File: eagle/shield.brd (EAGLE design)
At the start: 68.6 x 53.3 mm, 31 parts, among them IC1 REG1117

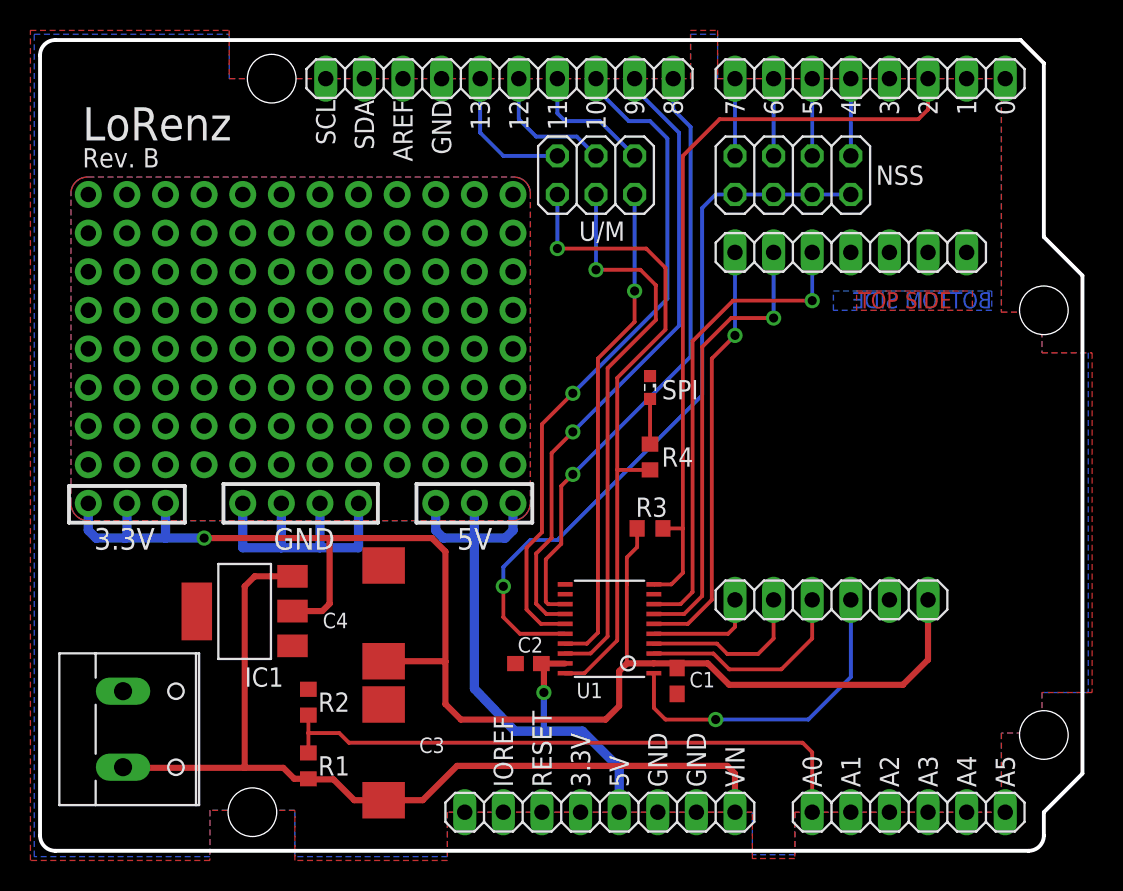
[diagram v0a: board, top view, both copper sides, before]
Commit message: Shield layout update
Added two separate TXB0104 instead of one TXB0108 (signal direction issues), added EN solder jumper for LED, removed battery level measurement, increased the protoyping area size, general layout changes for easier soldering.
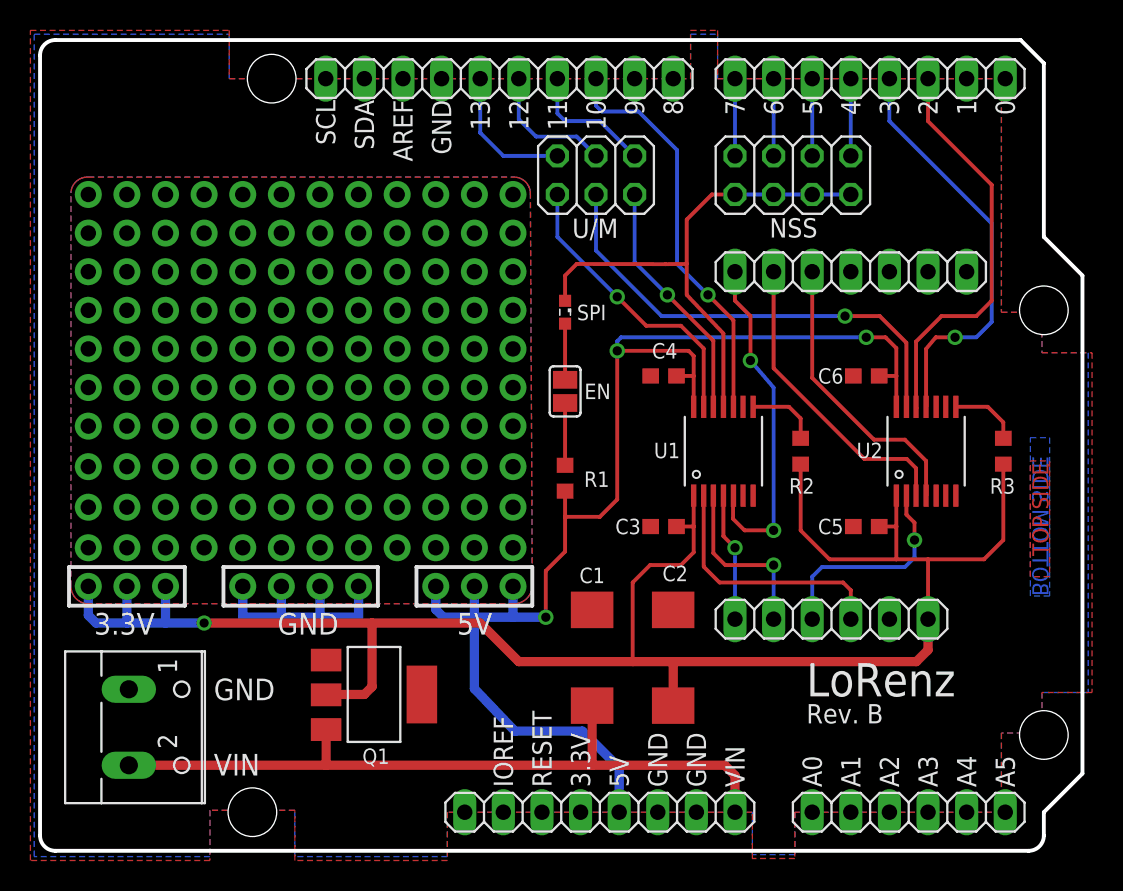
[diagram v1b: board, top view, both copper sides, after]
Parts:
- removed IC1: REG1117, burr-brown:SOT223
- removed R4: 1k, rcl:R0603
- removed U$1: PINHD-1X4, adafruit:1X04-CLEANBIG
- added C5, C6: 0.1 uF, rcl:C0603
- added EN: (no value), jumper:SJ
- added JP10: (no value), adafruit:1X12-CB
- added JP12: PINHD-1X4, adafruit:1X04-CLEANBIG
- added JP13: (no value), adafruit:1X03-CLEANBIG
- added Q1: REG1117, burr-brown:SOT223
- added U2: TXB0104PWR, Texas Instruments_By_element14_Batch_1:SOP65P640X120-14N
- C1, C2: value 0.1 uF -> 100 uF; device rcl:C0603 -> rcl:SMC_D
- C3, C4: value 100 uF -> 0.1 uF; device rcl:SMC_D -> rcl:C0603
- JP9: device adafruit:1X03-CLEANBIG -> adafruit:1X12-CB
- R1: value 3M3 -> 1k
- R2: value 1M -> 10k
- U1: value (none) -> TXB0104PWR; device adafruit:TSSOP20 -> Texas Instruments_By_element14_Batch_1:SOP65P640X120-14N
- moved R2 36.4 mm to (50.2, 26.4), turned to 90 degrees
- moved R1 25.4 mm to (34.7, 24.6), turned to 90 degrees
- moved C4 24.1 mm to (41.1, 31.4), turned to 0 degrees
- moved R3 23.8 mm to (63.5, 26.4), turned to 90 degrees
- moved C3 23.7 mm to (41.1, 21.5), turned to 0 degrees
- moved U1 13.9 mm to (45.1, 26.4)
- moved JP9 11.4 mm to (17.3, 22.7)
- moved C2 9.53 mm to (41.8, 12.8), turned to 90 degrees
- moved SPI 7.47 mm to (34.7, 35.6)
- moved C1 5.79 mm to (36.4, 12.8), turned to 90 degrees
- moved JP11 5.46 mm to (28.7, 17.5)
- moved LORA2 1.27 mm to (53.5, 38.2)
- moved LORA1 1.27 mm to (52.2, 15.4)
- moved POWER1 0.40 mm to (7.24, 8.26)
- moved JP8 0.13 mm to (17.3, 25.4)
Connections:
- removed net 3V3: C1.1, C4.+, IC1.2, JP9.1, JP9.2, JP9.3, LORA1.6, R3.1, U1.2
- removed net 5V: ARDUINO-LU.5, C2.1, JP11.1, JP11.2, JP11.3, U1.19
- removed net A0: ARDUINO-LD.1, R1.1, R2.2
- removed net OE: ARDUINO-RD.6, R3.2, U1.10
- new net +3V3: C2.+, C3.2, C5.2, JP13.1, JP13.2, JP13.3, LORA1.6, Q1.2, R2.1, R3.1, U1.1, U2.1
- new net +5V: ARDUINO-LU.5, C4.2, C6.2, JP11.1, JP11.2, JP11.3, R1.1, U1.14, U2.14
- new net N$10: EN.1, R1.2
- new net N$11: R2.2, U1.8
- new net N$12: R3.2, U2.8
- net A_DIO0: now also ARDUINO-RD.6, U2.12; no longer ARDUINO-RU.9, U1.14
- net A_DIO1: now also ARDUINO-RD.5, U2.11; no longer ARDUINO-RU.10, U1.13
- net A_MISO: now also U2.13; no longer U1.18
- net A_MOSI: now also U1.12; no longer U1.17
- net A_NSS: now also SPI.C, U1.11; no longer U1.16
- net A_RESET: now also U1.10; no longer U1.15
- net A_SCK: now also U1.13; no longer R4.2, U1.20
- net GND: now also C1.-, C2.-, C3.1, C4.1, C5.1, C6.1, JP12.1, JP12.2, JP12.3, JP12.4, Q1.1, U1.7, U2.7; no longer C1.2, C2.2, C3.-, C4.-, IC1.1, R2.1, SPI.C, U$1.1, U$1.2, U$1.3, U$1.4, U1.11
- net L_DIO0: now also U2.3; no longer U1.7
- net L_DIO1: now also U2.4; no longer U1.8
- net L_MISO: now also U2.2; no longer U1.3
- net L_MOSI: now also U1.3; no longer U1.4
- net L_NSS: now also U1.4; no longer U1.5
- net L_RESET: now also U1.5; no longer U1.6
- net L_SCK: now also U1.2; no longer U1.1
- net N$4: now also EN.2; no longer R4.1
- net VIN: now also C1.+, Q1.3; no longer C3.+, IC1.3, R1.2
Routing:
- net +3V3: track 0.00 -> 124.1 mm, vias 0 -> 1
- net 3V3: track 101.4 -> 0.00 mm, vias 1 -> 0
- net +5V: track 0.00 -> 88.9 mm, vias 0 -> 3
- net OE: track 50.4 -> 0.00 mm
- net 5V: track 42.0 -> 0.00 mm, vias 1 -> 0
- net A0: track 40.2 -> 0.00 mm
- net A_SCK: track 43.5 -> 19.3 mm
- net A_RESET: track 44.5 -> 26.7 mm
- net A_MOSI: track 32.3 -> 16.1 mm
- net A_DIO0: track 41.8 -> 26.8 mm, vias 1 -> 0
- net A_NSS: track 48.0 -> 34.7 mm, vias 1 -> 0
- net L_DIO1: track 31.5 -> 19.0 mm, vias 1 -> 0
- net A_DIO1: track 40.2 -> 27.7 mm
- net VIN: track 60.2 -> 48.8 mm
- net L_DIO0: track 29.9 -> 20.3 mm, vias 1 -> 0
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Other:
- board text added: "C:/Users/Honza/Desktop/ATLAS/atlas_logo_notext_gs.bmp"

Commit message: Shield and breakout layout update
Added a gap to the pin headers on LoRa breakout board and the shield to enforce breakout orientation.
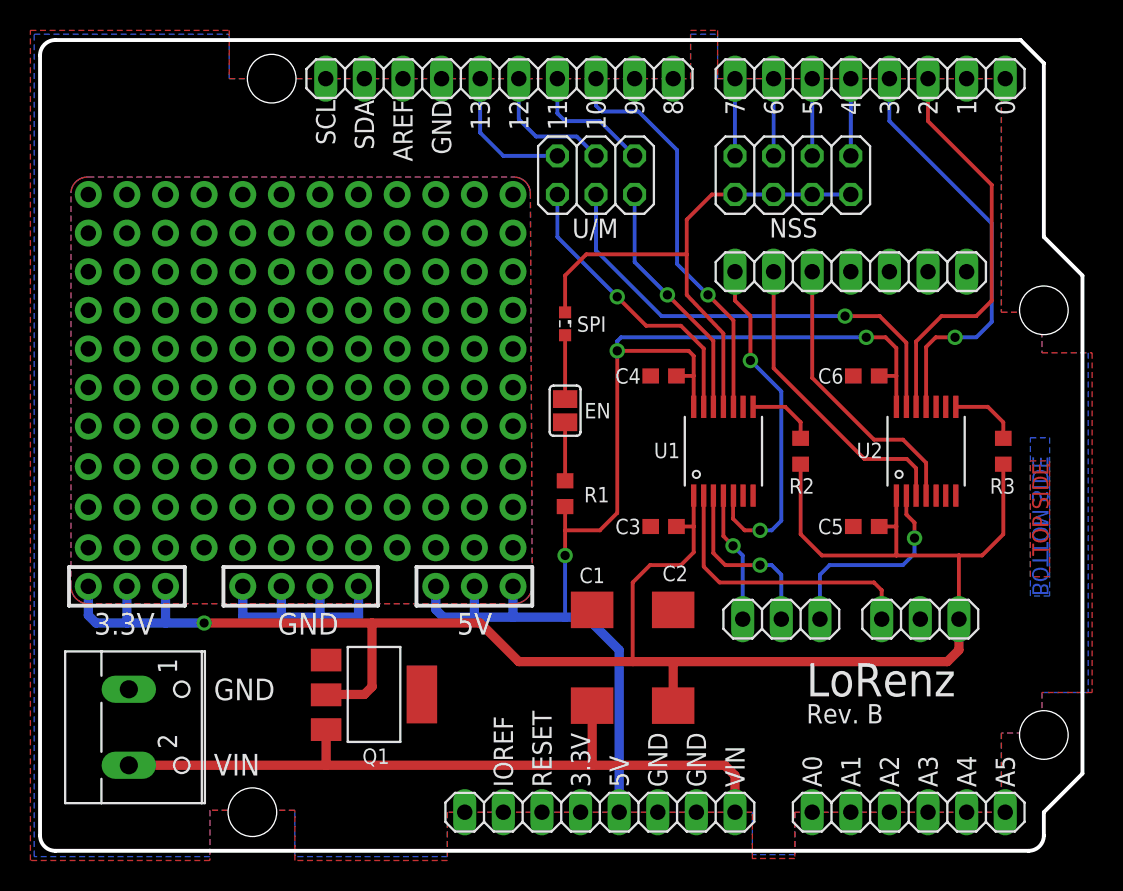
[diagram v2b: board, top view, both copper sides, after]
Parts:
- removed LORA1: (no value), pinhead:1X06
- added LORA1A, LORA1B: (no value), pinhead:1X03
- moved EN 1.27 mm to (34.7, 29.1)
- moved R1 1.02 mm to (34.7, 23.6)
- moved SPI 0.76 mm to (34.7, 34.8)
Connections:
- net +3V3: now also LORA1B.3; no longer LORA1.6
- net GND: now also LORA1B.2; no longer LORA1.5
- net L_MISO: now also LORA1A.3; no longer LORA1.3
- net L_MOSI: now also LORA1A.2; no longer LORA1.2
- net L_NSS: now also LORA1A.1; no longer LORA1.1
- net L_SCK: now also LORA1B.1; no longer LORA1.4
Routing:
- net +5V: track 88.9 -> 85.3 mm
- net L_SCK: track 16.9 -> 18.9 mm
- net +3V3: track 124.1 -> 125.8 mm
- net A_NSS: track 34.7 -> 35.8 mm
- net L_MISO: track 14.3 -> 13.8 mm
- net N$4: track 3.70 -> 4.20 mm

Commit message: Changed package of C2
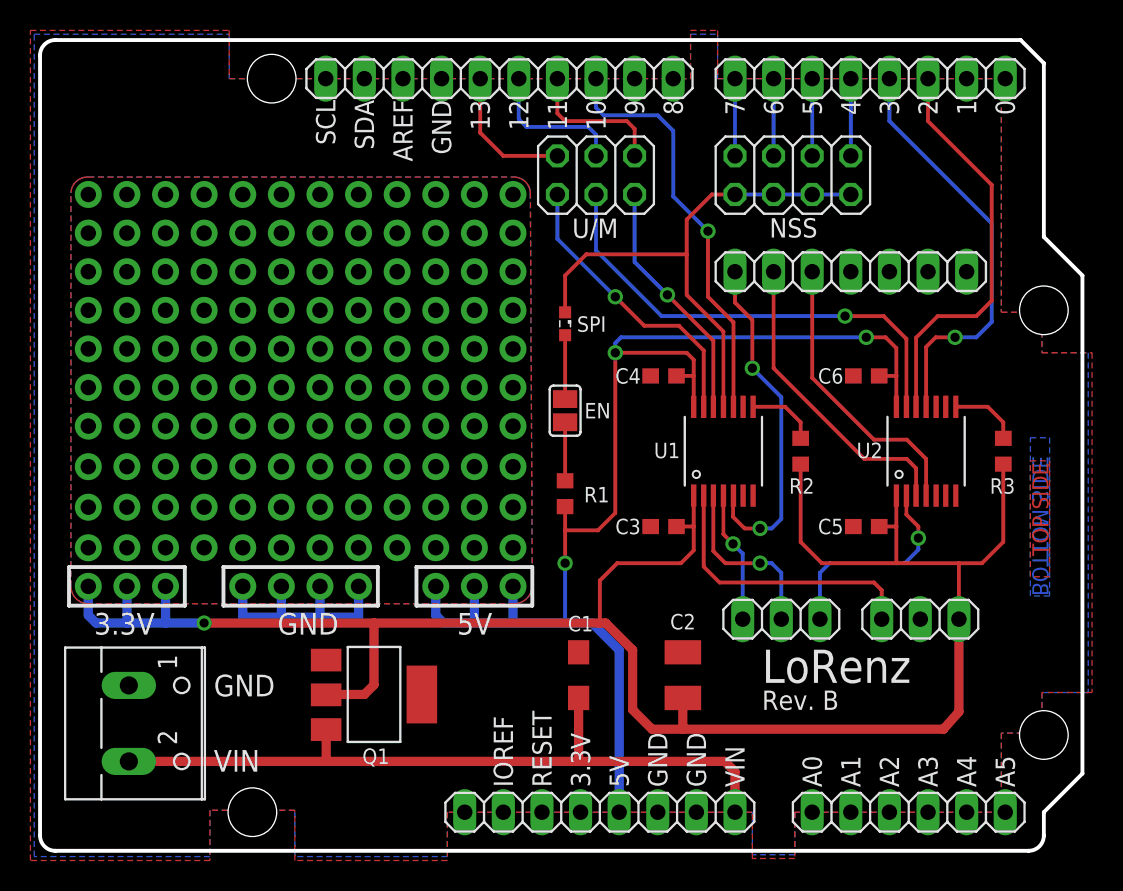
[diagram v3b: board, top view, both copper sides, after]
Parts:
- C1: value 100 uF -> 10 uF; device rcl:SMC_D -> rcl:SMC_A
- C2: device rcl:SMC_D -> rcl:SMC_B
- moved C1 1.45 mm to (35.6, 11.7)
- moved C2 1.31 mm to (42.4, 11.7)
- moved POWER1 0.25 mm to (7.24, 8.51)
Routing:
- net +3V3: track 125.8 -> 134.1 mm
- net +5V: track 85.3 -> 86.5 mm
- net A_MOSI_UNO: track 8.52 -> 9.56 mm
- net A_MISO_UNO: track 8.75 -> 9.56 mm
- net A_RESET: track 26.7 -> 27.4 mm

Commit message: Major layout update, read details
The layouts of shield and all breakout boards were changed to match the new multiprotocol standard.
IMPORTANT: The new shield is NOT compatible with the old breakout boards!
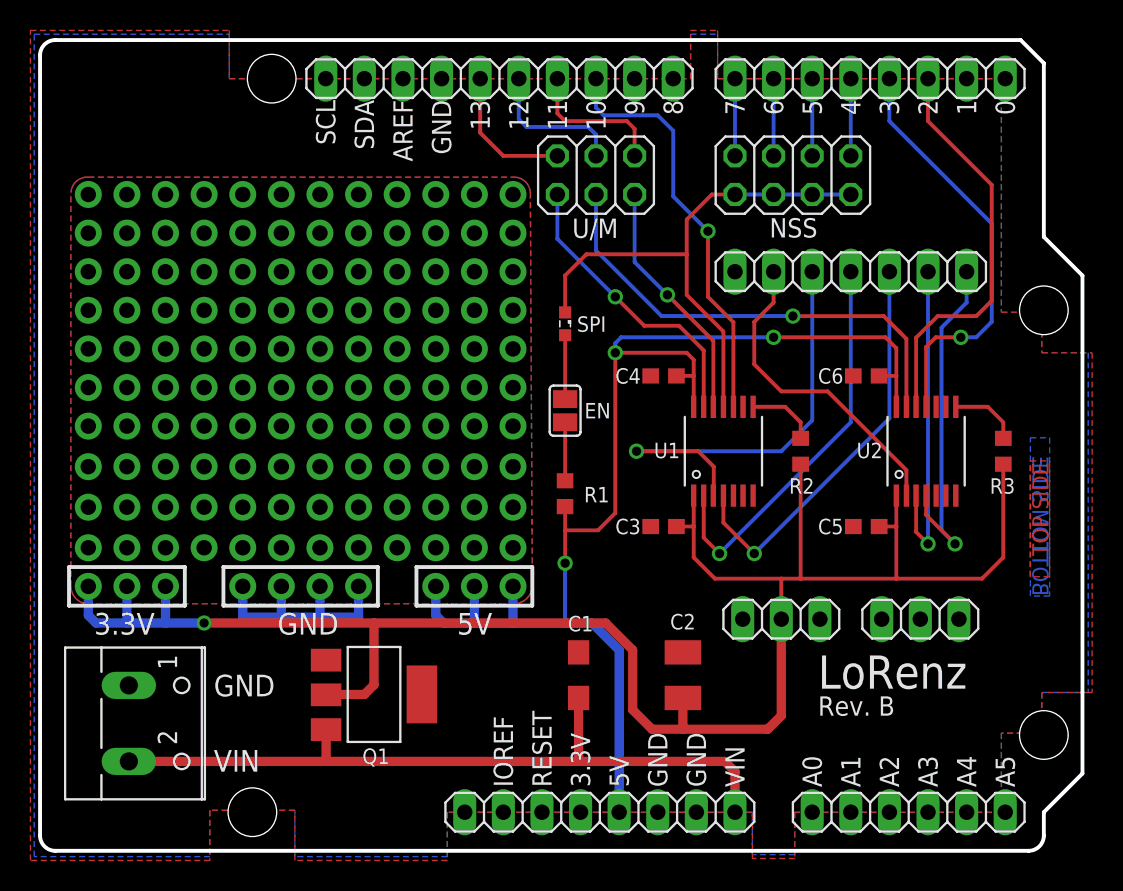
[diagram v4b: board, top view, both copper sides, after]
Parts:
- renumbered LORA1A to CON_0, LORA1B to CON_1, LORA2 to CON_2
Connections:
- net +3V3: now also CON_0.2; no longer CON_1.3
- net GND: now also CON_0.3; no longer CON_1.2
- net L_DIO0: now also CON_2.6; no longer CON_2.2
- net L_DIO1: now also CON_2.7; no longer CON_2.3
- net L_MISO: now also CON_2.2; no longer CON_0.3
- net L_MOSI: now also CON_2.3; no longer CON_0.2
- net L_NSS: now also CON_2.5; no longer CON_0.1
- net L_RESET: no longer CON_2.1
- net L_SCK: now also CON_2.4; no longer CON_1.1
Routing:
- net L_RESET: track 22.7 -> 0.00 mm, vias 2 -> 0
- net L_NSS: track 8.65 -> 26.9 mm
- net L_MOSI: track 11.8 -> 29.6 mm
- net +3V3: track 134.1 -> 123.6 mm
- net L_SCK: track 18.9 -> 26.4 mm, vias 0 -> 1
- net L_MISO: track 14.0 -> 21.2 mm, vias 1 -> 0
- net L_DIO1: track 19.1 -> 22.9 mm, vias 0 -> 1
- net L_DIO0: track 20.3 -> 21.4 mm, vias 0 -> 1

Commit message: Release 1.0
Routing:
- net L_MOSI: track 29.6 -> 19.7 mm
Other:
- board text added: "+"
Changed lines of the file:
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@@
 <rectangle x1="7.508875" y1="51.520725" x2="7.515225" y2="51.527075" layer="200"/>
 <text x="0" y="-0.03175" size="0.0127" layer="200" font="vector">C:/Users/Honza/Desktop/ATLAS/atlas_logo_notext_gs.bmp</text>
+<text x="36.83" y="10.033" size="1.016" layer="25">+</text>
+<text x="44.323" y="9.906" size="1.016" layer="25">+</text>
 </plain>
 <attributes>
@@
 <wire x1="50.927" y1="38.227" x2="50.927" y2="28.448" width="0.254" layer="16"/>
 <wire x1="50.927" y1="28.448" x2="48.895" y2="26.416" width="0.254" layer="16"/>
-<wire x1="48.895" y1="26.416" x2="39.37" y2="26.416" width="0.254" layer="16"/>
-<via x="39.37" y="26.416" extent="1-16" drill="0.6096"/>
-<wire x1="39.37" y1="26.416" x2="43.434" y2="26.416" width="0.254" layer="1"/>
-<wire x1="43.434" y1="26.416" x2="44.45" y2="25.4" width="0.254" layer="1"/>
-<wire x1="44.45" y1="25.4" x2="44.45" y2="23.5204" width="0.254" layer="1"/>
+<wire x1="48.895" y1="26.416" x2="46.736" y2="26.416" width="0.254" layer="16"/>
+<via x="46.736" y="26.416" extent="1-16" drill="0.6096"/>
+<wire x1="46.736" y1="26.416" x2="45.085" y2="26.416" width="0.254" layer="1"/>
+<wire x1="45.085" y1="26.416" x2="44.45" y2="25.781" width="0.254" layer="1"/>
+<wire x1="44.45" y1="25.781" x2="44.45" y2="23.5204" width="0.254" layer="1"/>
 <wire x1="44.45" y1="23.5204" x2="44.4246" y2="23.495" width="0.254" layer="1"/>
 </signal>
